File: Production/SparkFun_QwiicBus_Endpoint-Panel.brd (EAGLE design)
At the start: 237.5 x 116.8 mm, 1077 parts, among them J1 QWIIC, J10 RJ45, J100 QWIIC, J101 RJ45, J106 QWIIC, J107 QWIIC, J108 RJ45, J15 QWIIC, J16 QWIIC, J17 RJ45, J2 QWIIC, J22 QWIIC, J23 QWIIC, J24 RJ45, J29 QWIIC, J3 RJ45, J30 QWIIC, J31 RJ45, J36 QWIIC, J37 QWIIC, J38 RJ45, J43 QWIIC, J44 QWIIC, J45 RJ45, J50 QWIIC, J51 QWIIC, J52 RJ45, J57 QWIIC, J58 QWIIC, J59 RJ45, J6 QWIIC, J64 QWIIC, J65 QWIIC, J66 RJ45, J71 QWIIC, J72 QWIIC, J73 RJ45, J78 QWIIC, J79 QWIIC, J80 RJ45, J85 QWIIC, J86 QWIIC, J87 RJ45, J9 QWIIC, J92 QWIIC, J93 QWIIC, J94 RJ45, J99 QWIIC, U1 PCA9615, U10 PCA9615, U11 PCA9615, U12 PCA9615, U13 PCA9615, U14 PCA9615, U15 PCA9615, U16 PCA9615, U2 PCA9615, U3 PCA9615, U4 PCA9615, U5 PCA9615, U6 PCA9615, U7 PCA9615, U8 PCA9615, U9 PCA9615

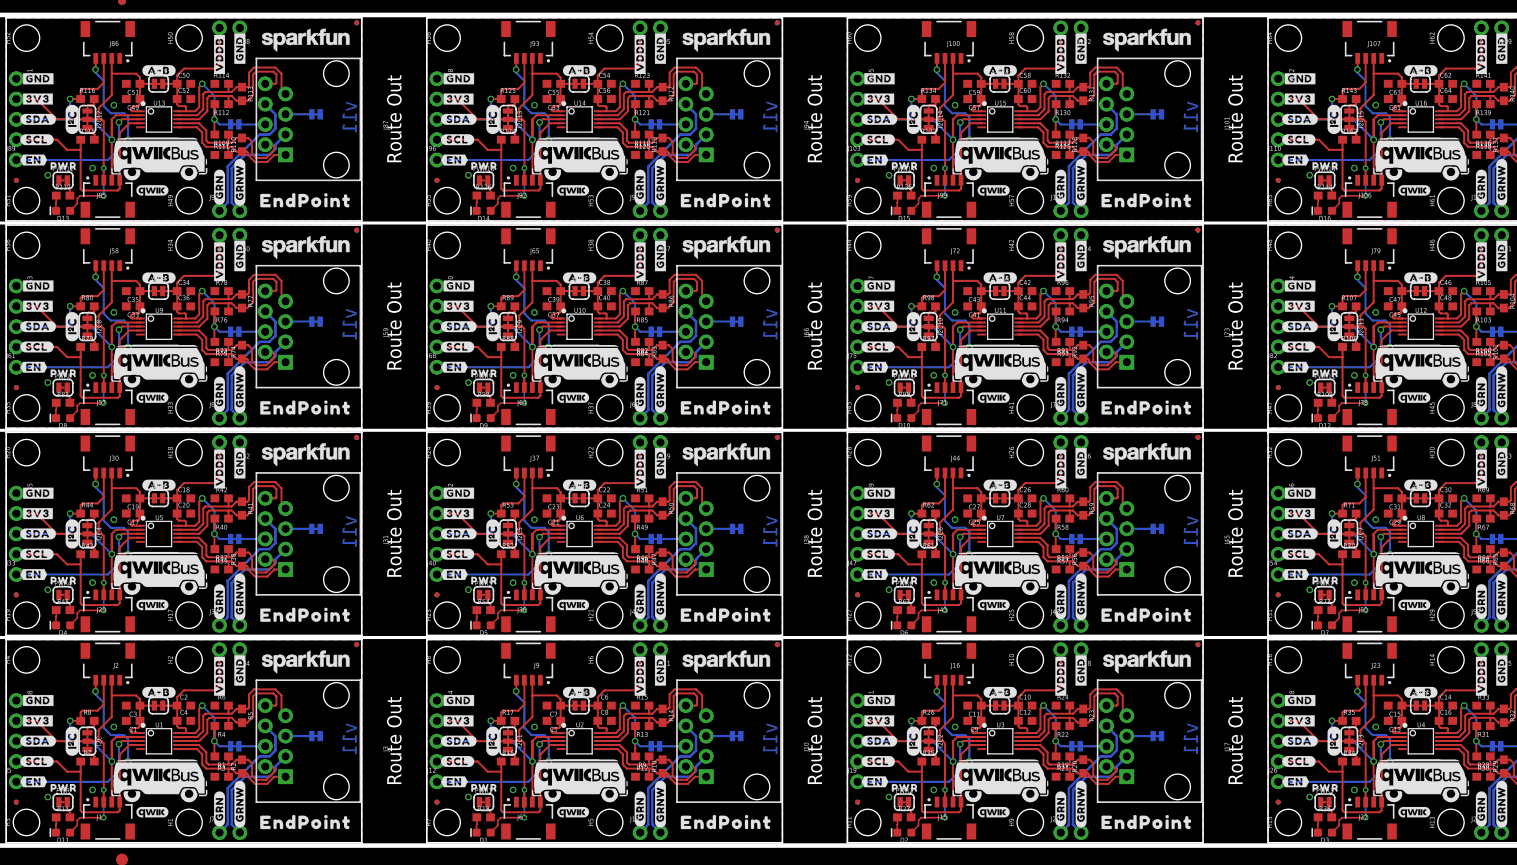
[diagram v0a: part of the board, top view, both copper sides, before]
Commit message: moving qwiicBus up a tad
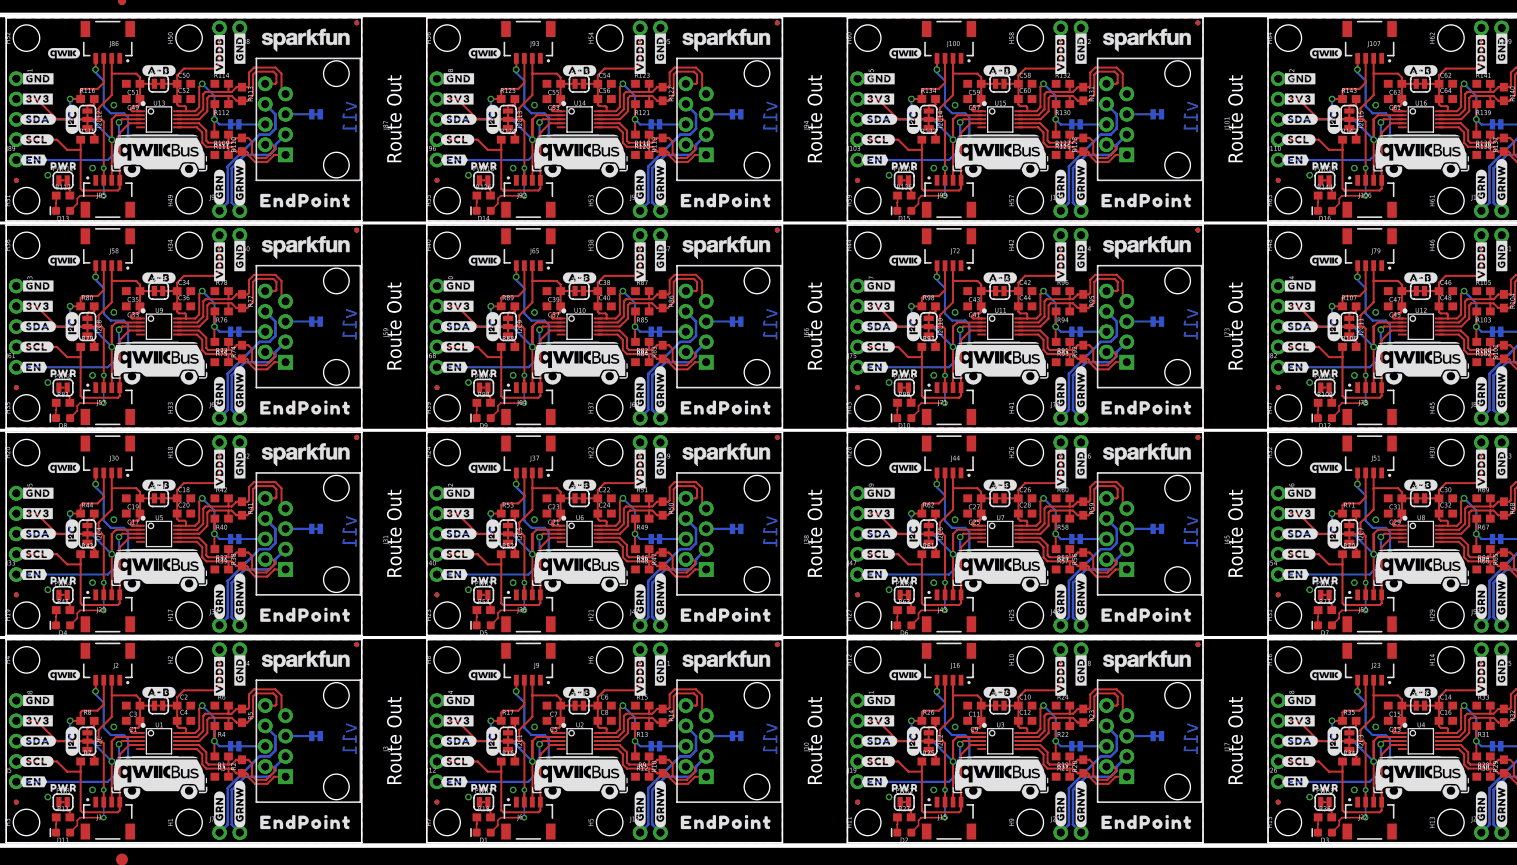
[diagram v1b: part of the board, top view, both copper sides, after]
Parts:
- moved LOGO54 20.4 mm to (112.4, 72.8)
- moved LOGO14 20.4 mm to (112.4, 21.0)
- moved LOGO34 20.4 mm to (112.4, 46.9)
- moved LOGO44 20.4 mm to (7.24, 72.8)
- moved LOGO49 20.4 mm to (59.8, 72.8)
- moved LOGO24 20.4 mm to (7.24, 46.9)
- moved LOGO29 20.4 mm to (59.8, 46.9)
- moved LOGO3 20.4 mm to (7.24, 21.0)
- moved LOGO74 20.4 mm to (112.4, 98.7)
- moved LOGO9 20.4 mm to (59.8, 21.0)
- moved LOGO64 20.4 mm to (7.24, 98.7)
- moved LOGO69 20.4 mm to (59.8, 98.7)
- moved LOGO19 20.4 mm to (165.0, 21.0)
- moved LOGO39 20.4 mm to (165.0, 46.9)
- moved LOGO59 20.4 mm to (165.0, 72.8)
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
